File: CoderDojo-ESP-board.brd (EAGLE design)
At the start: 100 x 80 mm, 85 parts, among them IC1 ESP-12E/F, IC2 FT232RL, IC3 L293D, U1 PCA9685PW,118, U2 AMS1117-3.3, U3 MCP23017-E/SO, X1 PN61729-S

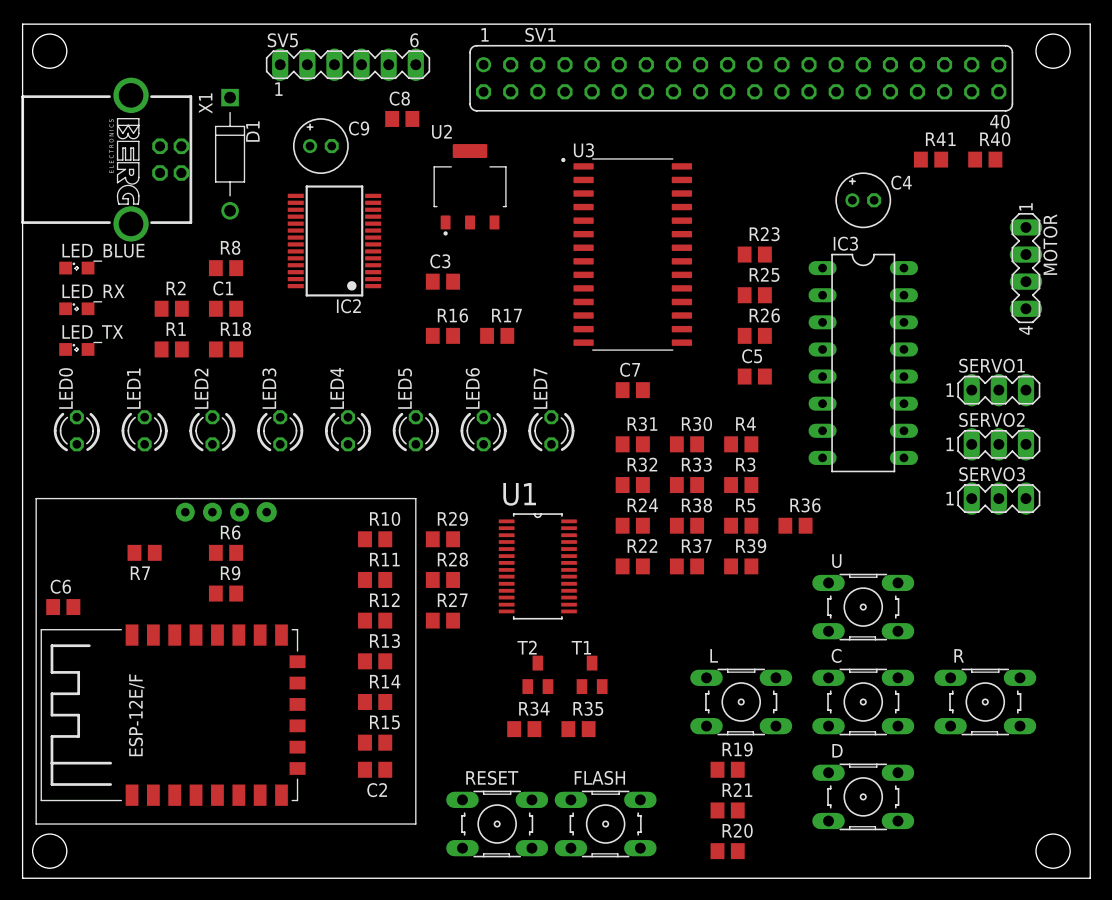
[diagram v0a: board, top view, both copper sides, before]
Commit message: place components to board + add transistor datasheet S8050
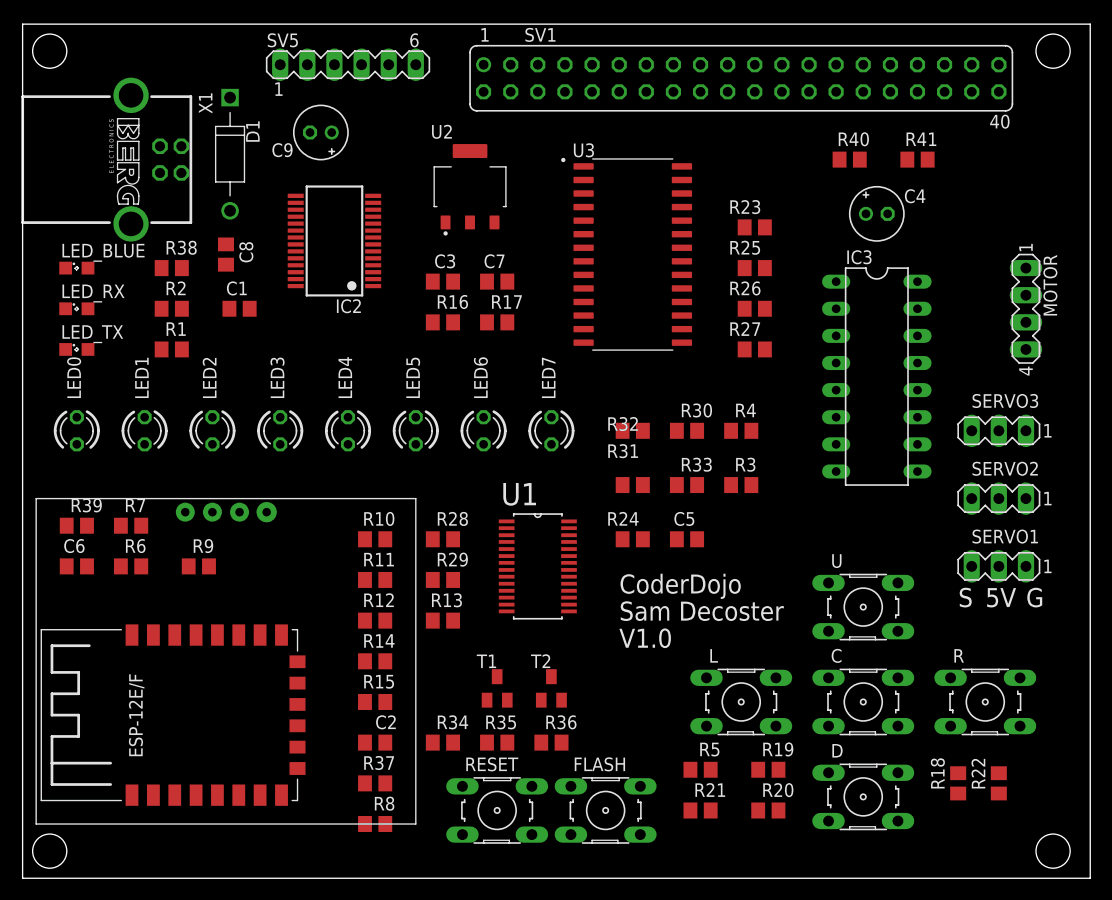
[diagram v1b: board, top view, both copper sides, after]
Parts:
- moved R18 79.7 mm to (87.6, 8.89), turned to 90 degrees
- moved R39 62.3 mm to (5.08, 33.0)
- moved R38 54.0 mm to (14.0, 57.1)
- moved R8 53.9 mm to (33.0, 5.08), turned to 180 degrees
- moved R22 39.9 mm to (91.4, 8.89), turned to 90 degrees
- moved R27 38.7 mm to (68.6, 49.5), turned to 180 degrees
- moved R37 35.6 mm to (33.0, 8.89), turned to 180 degrees
- moved R36 30.6 mm to (49.5, 12.7)
- moved R5 23.2 mm to (63.5, 10.2), turned to 180 degrees
- moved C8 20.8 mm to (19.1, 58.4), turned to 270 degrees
- moved C5 16.5 mm to (62.2, 31.8)
- moved SERVO1 16.5 mm to (91.4, 29.2), turned to 180 degrees
- moved C7 16.3 mm to (44.5, 55.9)
- moved R40 12.7 mm to (77.5, 67.3), turned to 180 degrees
- moved R6 8.98 mm to (10.2, 29.2)
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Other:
- board text added: "5V"
- board text added: "CoderDojo"
- board text added: "G"
- board text added: "S"
- board text added: "Sam Decoster"
- board text added: "V1.0"

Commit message: before routing
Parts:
- moved R4 37.8 mm to (39.4, 16.5)
- moved R3 32.5 mm to (39.4, 20.3)
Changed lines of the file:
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@@
 <attribute name="VALUE" x="38.735" y="25.4" size="1.27" layer="27"/>
 </element>
-<element name="R3" library="rcl" library_urn="urn:adsk.eagle:library:334" package="R0805" package3d_urn="urn:adsk.eagle:package:23553/2" value="4K7" x="67.31" y="36.83" smashed="yes">
-<attribute name="NAME" x="66.675" y="38.1" size="1.27" layer="25"/>
-<attribute name="POPULARITY" value="86" x="152.4" y="-48.26" size="1.778" layer="27" display="off"/>
-<attribute name="SPICEPREFIX" value="R" x="152.4" y="-48.26" size="1.778" layer="27" display="off"/>
-<attribute name="VALUE" x="66.675" y="34.29" size="1.27" layer="27"/>
+<element name="R3" library="rcl" library_urn="urn:adsk.eagle:library:334" package="R0805" package3d_urn="urn:adsk.eagle:package:23553/2" value="4K7" x="39.37" y="20.32" smashed="yes">
+<attribute name="NAME" x="38.735" y="21.59" size="1.27" layer="25"/>
+<attribute name="POPULARITY" value="86" x="124.46" y="-64.77" size="1.778" layer="27" display="off"/>
+<attribute name="SPICEPREFIX" value="R" x="124.46" y="-64.77" size="1.778" layer="27" display="off"/>
+<attribute name="VALUE" x="38.735" y="17.78" size="1.27" layer="27"/>
 </element>
 <element name="R30" library="rcl" library_urn="urn:adsk.eagle:library:334" package="R0805" package3d_urn="urn:adsk.eagle:package:23553/2" value="10K" x="62.23" y="41.91" smashed="yes">
@@
 <attribute name="VALUE" x="4.445" y="30.48" size="1.27" layer="27"/>
 </element>
-<element name="R4" library="rcl" library_urn="urn:adsk.eagle:library:334" package="R0805" package3d_urn="urn:adsk.eagle:package:23553/2" value="4K7" x="67.31" y="41.91" smashed="yes">
-<attribute name="NAME" x="66.675" y="43.18" size="1.27" layer="25"/>
-<attribute name="POPULARITY" value="86" x="157.48" y="-43.18" size="1.778" layer="27" display="off"/>
-<attribute name="SPICEPREFIX" value="R" x="157.48" y="-43.18" size="1.778" layer="27" display="off"/>
-<attribute name="VALUE" x="66.675" y="39.37" size="1.27" layer="27"/>
+<element name="R4" library="rcl" library_urn="urn:adsk.eagle:library:334" package="R0805" package3d_urn="urn:adsk.eagle:package:23553/2" value="4K7" x="39.37" y="16.51" smashed="yes">
+<attribute name="NAME" x="38.735" y="17.78" size="1.27" layer="25"/>
+<attribute name="POPULARITY" value="86" x="129.54" y="-68.58" size="1.778" layer="27" display="off"/>
+<attribute name="SPICEPREFIX" value="R" x="129.54" y="-68.58" size="1.778" layer="27" display="off"/>
+<attribute name="VALUE" x="38.735" y="13.97" size="1.27" layer="27"/>
 </element>
 <element name="R40" library="rcl" library_urn="urn:adsk.eagle:library:334" package="R0805" package3d_urn="urn:adsk.eagle:package:23553/2" value="220K" x="77.47" y="67.31" smashed="yes" rot="R180">
@@
 <contactref element="SV1" pad="1"/>
 <wire x1="52.545" y1="51.435" x2="43.18" y2="76.2" width="0" layer="19" extent="1-1"/>
-<wire x1="66.36" y1="41.91" x2="52.545" y2="51.435" width="0" layer="19" extent="1-1"/>
-<wire x1="51.181" y1="32.7914" x2="66.36" y2="41.91" width="0" layer="19" extent="1-1"/>
+<wire x1="38.42" y1="16.51" x2="52.545" y2="51.435" width="0" layer="19" extent="1-1"/>
+<wire x1="51.181" y1="32.7914" x2="38.42" y2="16.51" width="0" layer="19" extent="1-1"/>
 <wire x1="22.86" y1="34.29" x2="51.181" y2="32.7914" width="0" layer="19" extent="1-1"/>
 <wire x1="16.25" y1="22.78" x2="22.86" y2="34.29" width="0" layer="19" extent="1-1"/>
@@
 <wire x1="52.545" y1="52.705" x2="45.72" y2="76.2" width="0" layer="19" extent="1-1"/>
 <wire x1="51.181" y1="32.131" x2="52.545" y2="52.705" width="0" layer="19" extent="1-1"/>
-<wire x1="66.36" y1="36.83" x2="51.181" y2="32.131" width="0" layer="19" extent="1-1"/>
+<wire x1="38.42" y1="20.32" x2="51.181" y2="32.131" width="0" layer="19" extent="1-1"/>
 <wire x1="20.32" y1="34.29" x2="51.181" y2="32.131" width="0" layer="19" extent="1-1"/>
 <wire x1="14.25" y1="22.78" x2="20.32" y2="34.29" width="0" layer="19" extent="1-1"/>
@@
 <wire x1="51.181" y1="33.4264" x2="49.53" y2="43.18" width="0" layer="19" extent="1-1"/>
 <wire x1="63.18" y1="31.75" x2="51.181" y2="33.4264" width="0" layer="19" extent="1-1"/>
-<wire x1="68.26" y1="36.83" x2="63.18" y2="31.75" width="0" layer="19" extent="1-1"/>
-<wire x1="68.26" y1="41.91" x2="68.26" y2="36.83" width="0" layer="19" extent="1-1"/>
-<wire x1="75.4888" y1="27.6606" x2="68.26" y2="36.83" width="0" layer="19" extent="1-1"/>
+<wire x1="40.32" y1="20.32" x2="63.18" y2="31.75" width="0" layer="19" extent="1-1"/>
+<wire x1="40.32" y1="16.51" x2="40.32" y2="20.32" width="0" layer="19" extent="1-1"/>
+<wire x1="75.4888" y1="27.6606" x2="40.32" y2="20.32" width="0" layer="19" extent="1-1"/>
 <wire x1="75.4888" y1="18.7706" x2="75.4888" y2="27.6606" width="0" layer="19" extent="1-1"/>
 <wire x1="75.4888" y1="9.8806" x2="75.4888" y2="18.7706" width="0" layer="19" extent="1-1"/>

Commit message: Routing PCB
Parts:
- moved R4 35.6 mm to (68.6, 36.8)
- moved R3 31.4 mm to (68.6, 31.8)
- moved R27 7.62 mm to (68.6, 41.9)
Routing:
- net GND: track 0.00 -> 479.6 mm, vias 0 -> 8
- net 3V3: track 0.00 -> 399.1 mm, vias 0 -> 3
- net ESP_RST: track 0.00 -> 187.8 mm, vias 0 -> 2
- net N$17: track 0.00 -> 168.0 mm, vias 0 -> 2
- net GPIO0: track 0.00 -> 156.6 mm, vias 0 -> 4
- net GPIO2: track 0.00 -> 150.0 mm, vias 0 -> 4
- net MISO: track 0.00 -> 147.1 mm, vias 0 -> 2
- net GPIO16: track 0.00 -> 145.8 mm, vias 0 -> 4
- net 5V: track 0.00 -> 141.5 mm, vias 0 -> 3
- net RXD: track 0.00 -> 140.7 mm
- net GPIO10: track 0.00 -> 139.3 mm, vias 0 -> 2
- net CS0: track 0.00 -> 138.9 mm, vias 0 -> 2
- net GPIO13: track 0.00 -> 135.5 mm
- net BTN_C: track 0.00 -> 133.5 mm, vias 0 -> 1
- net SCL: track 0.00 -> 125.5 mm, vias 0 -> 6
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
